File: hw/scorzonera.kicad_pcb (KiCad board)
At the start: 2 copper layers, 70.7 x 53.3 mm, 23 parts, among them J1 NEIGHBOR1, J2 NEIGHBOR2, J3 Conn_01x05, J7 BONUS_ROW, U1 AM7969, U2 74ALVC164245, U3 MAX3232, Y1 Crystal_GND24

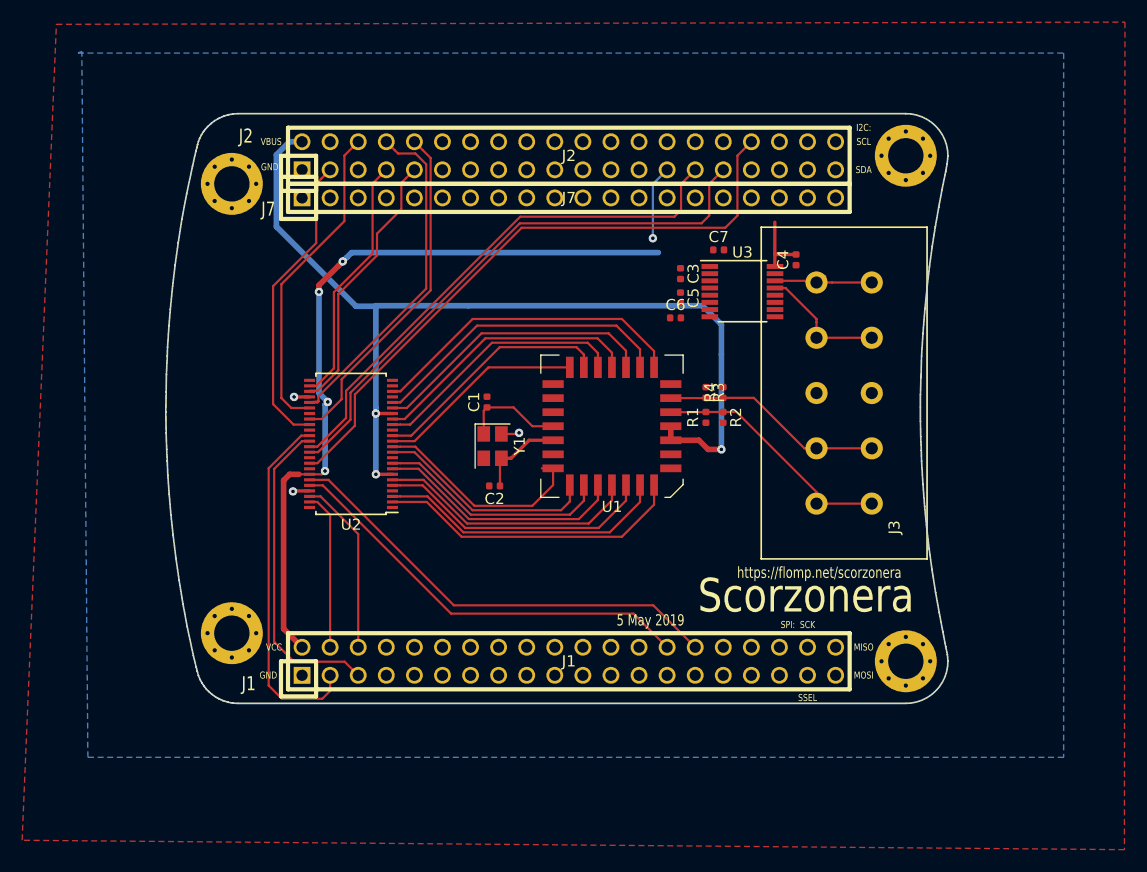
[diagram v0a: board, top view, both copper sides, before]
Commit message: Switch to 2 level shifters, caps, route, silk
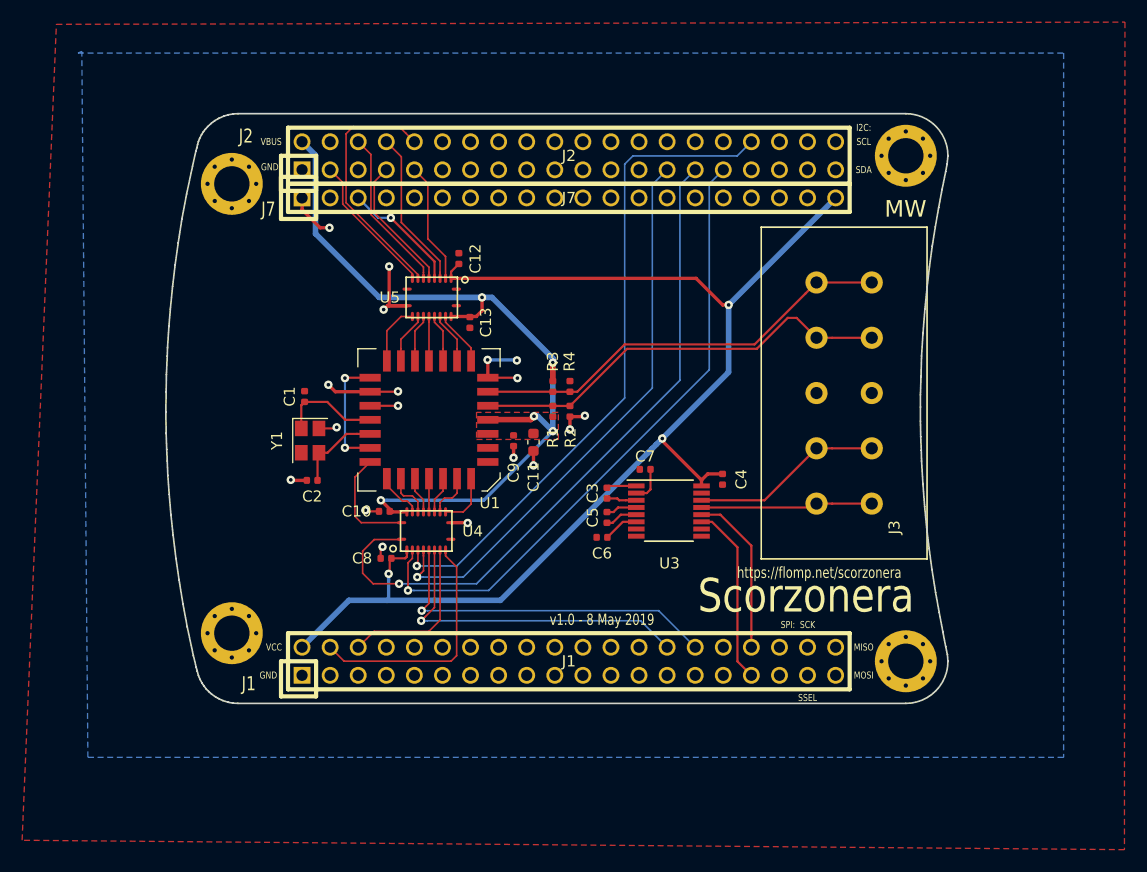
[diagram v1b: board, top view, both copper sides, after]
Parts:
- removed U2: 74ALVC164245, Package_SO:TSSOP-48_6.1x12.5mm_P0.5mm
- added C10: 100n, Capacitor_SMD:C_0402_1005Metric, F.Cu at (129.4, 104.5)
- added C11: 1u, Capacitor_SMD:C_0603_1608Metric, F.Cu at (142.8, 98.3)
- added C12: 100n, Capacitor_SMD:C_0402_1005Metric, F.Cu at (136.1, 81.7)
- added C13: 100n, Capacitor_SMD:C_0402_1005Metric, F.Cu at (137.1, 87.5)
- added C8: 100n, Capacitor_SMD:C_0402_1005Metric, F.Cu at (129.5, 108.8)
- added C9: 100n, Capacitor_SMD:C_0402_1005Metric, F.Cu at (141.1, 98.2)
- added U4: TXS0108EPW, wago:Texas_R-PVQFN-N20_4.65x3.65x1mm, F.Cu at (133.2, 106.3)
- added U5: TXS0108EPW, wago:Texas_R-PVQFN-N20_4.65x3.65x1mm, F.Cu at (133.7, 85.2)
- C1, C2: value C -> 18p
- moved C3 20.9 mm to (149.5, 102.9)
- moved C4 20.9 mm to (159.9, 101.7)
- moved U3 20.9 mm to (155.1, 104.5)
- moved C5 20.9 mm to (149.5, 105.1)
- moved C6 20.9 mm to (149.1, 106.9)
- moved C7 20.9 mm to (152.9, 100.8)
- moved U1 16.6 mm to (133.4, 96.3)
- moved C2 16.5 mm to (122.8, 101.8)
- moved C1 16.5 mm to (122.2, 94.2)
- moved Y1 16.5 mm to (122.7, 98.2)
- moved R1 13.9 mm to (144.6, 95.5)
- moved R2 13.9 mm to (146.2, 95.5)
- moved R3 13.9 mm to (144.6, 93.2)
- moved R4 13.9 mm to (146.2, 93.2)
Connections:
- J1 pad 33: /P9_5 -> /U0_TXD
- J1 pad 34: /P9_6 -> /U0_RXD
- J1 pad 5: /SGPIO15 -> /notSGPIO15
- J2 pad 13: /P2_8 -> /SGPIO15
- J3 pad 1: /SERIN+ -> /RS232_RX
- J3 pad 2: /SERIN- -> /RS232_TX
- J3 pad 4: /RS232_RX -> /SERIN+
- J3 pad 5: /RS232_TX -> /SERIN-
- U3 pad 11: /U1_TXD -> /U0_TXD
- U3 pad 12: /U1_RXD -> /U0_RXD
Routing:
- net /SGPIO4: track 6.72 -> 51.3 mm
- net VCC: track 75.0 -> 110.4 mm, vias 4 -> 3
- net GND: track 4.56 -> 39.7 mm, vias 3 -> 18
- net /SGPIO14: track 32.3 -> 0.00 mm
- net /SGPIO15: track 28.7 -> 0.00 mm
- net /DSTRB: track 29.0 -> 4.98 mm
- net /CSTRB: track 27.8 -> 4.66 mm
- net /DO0: track 27.9 -> 4.90 mm
- net /DO1: track 26.4 -> 4.05 mm
- net /DO2: track 25.1 -> 3.32 mm
- net /VLTN: track 26.1 -> 4.34 mm
- net /DO3: track 23.7 -> 3.00 mm
- net /CO0: track 24.7 -> 4.03 mm
- net /DO4: track 22.5 -> 3.32 mm
- net /CO1: track 23.3 -> 4.34 mm
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- added copper zone on F.Cu, net +5V
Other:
- net class smol added: clearance 0.15, trace_width 0.15, via_dia 0.762, via_drill 0.3302
- board text added: "MW"
- board text added: "v1.0 - 8 May 2019"
- board text removed: "5 May 2019"
